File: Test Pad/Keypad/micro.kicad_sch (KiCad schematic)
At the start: 9 parts

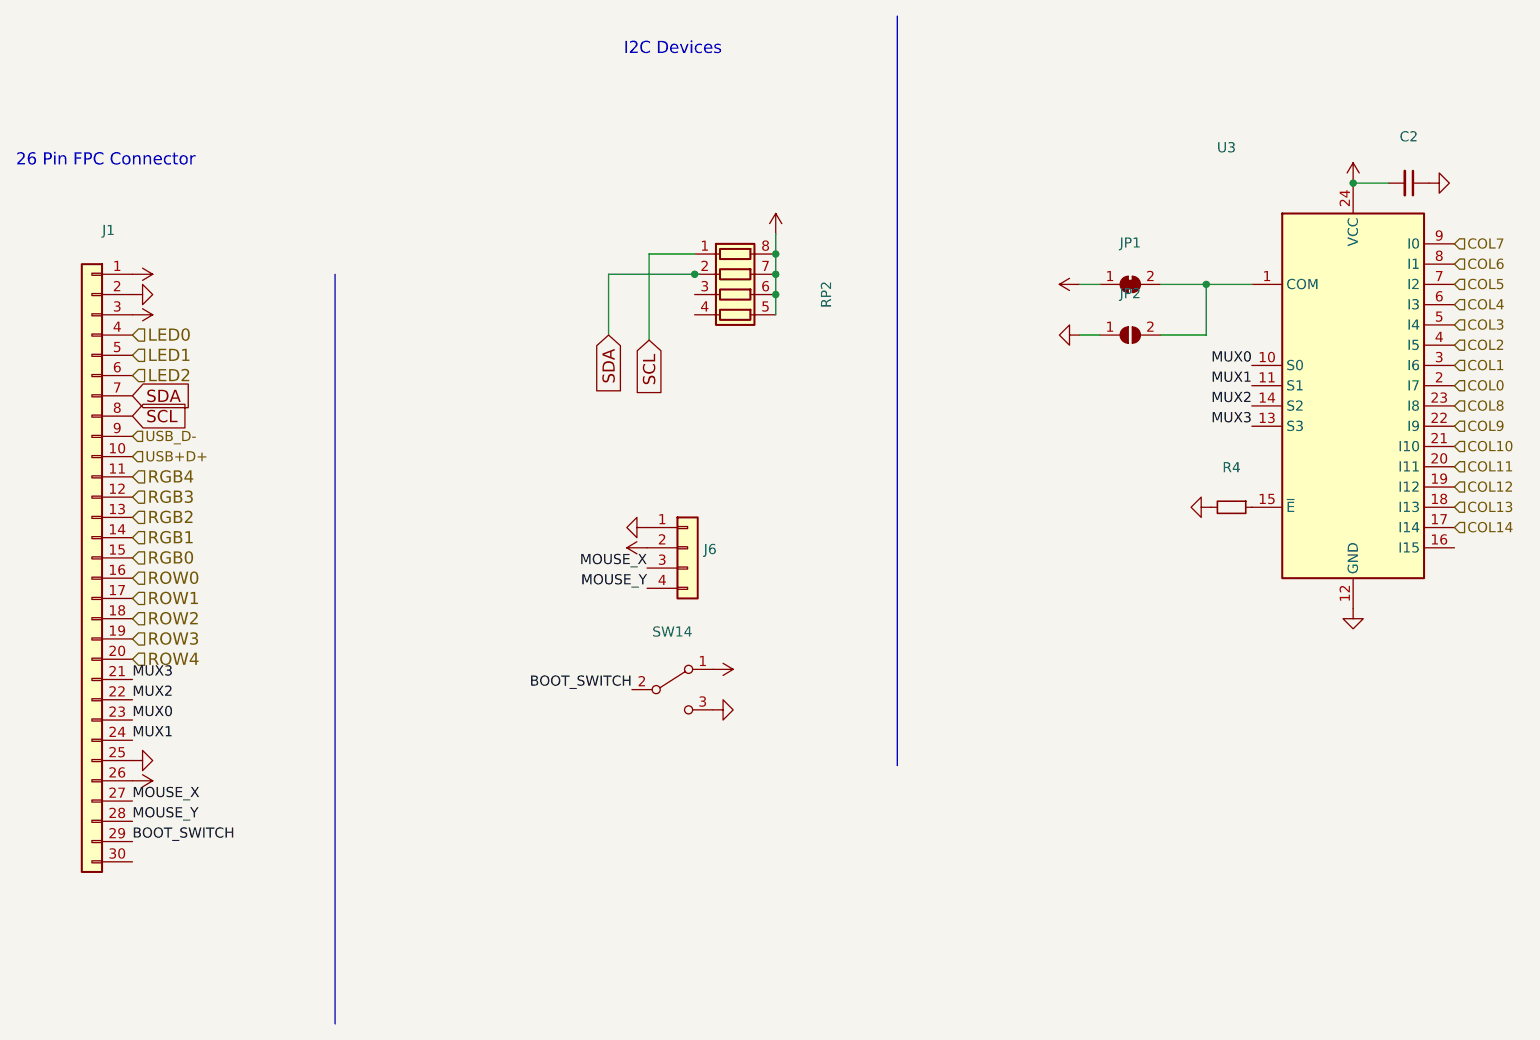
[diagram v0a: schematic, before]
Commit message: Started nucleo 144 test pad and keypad boards
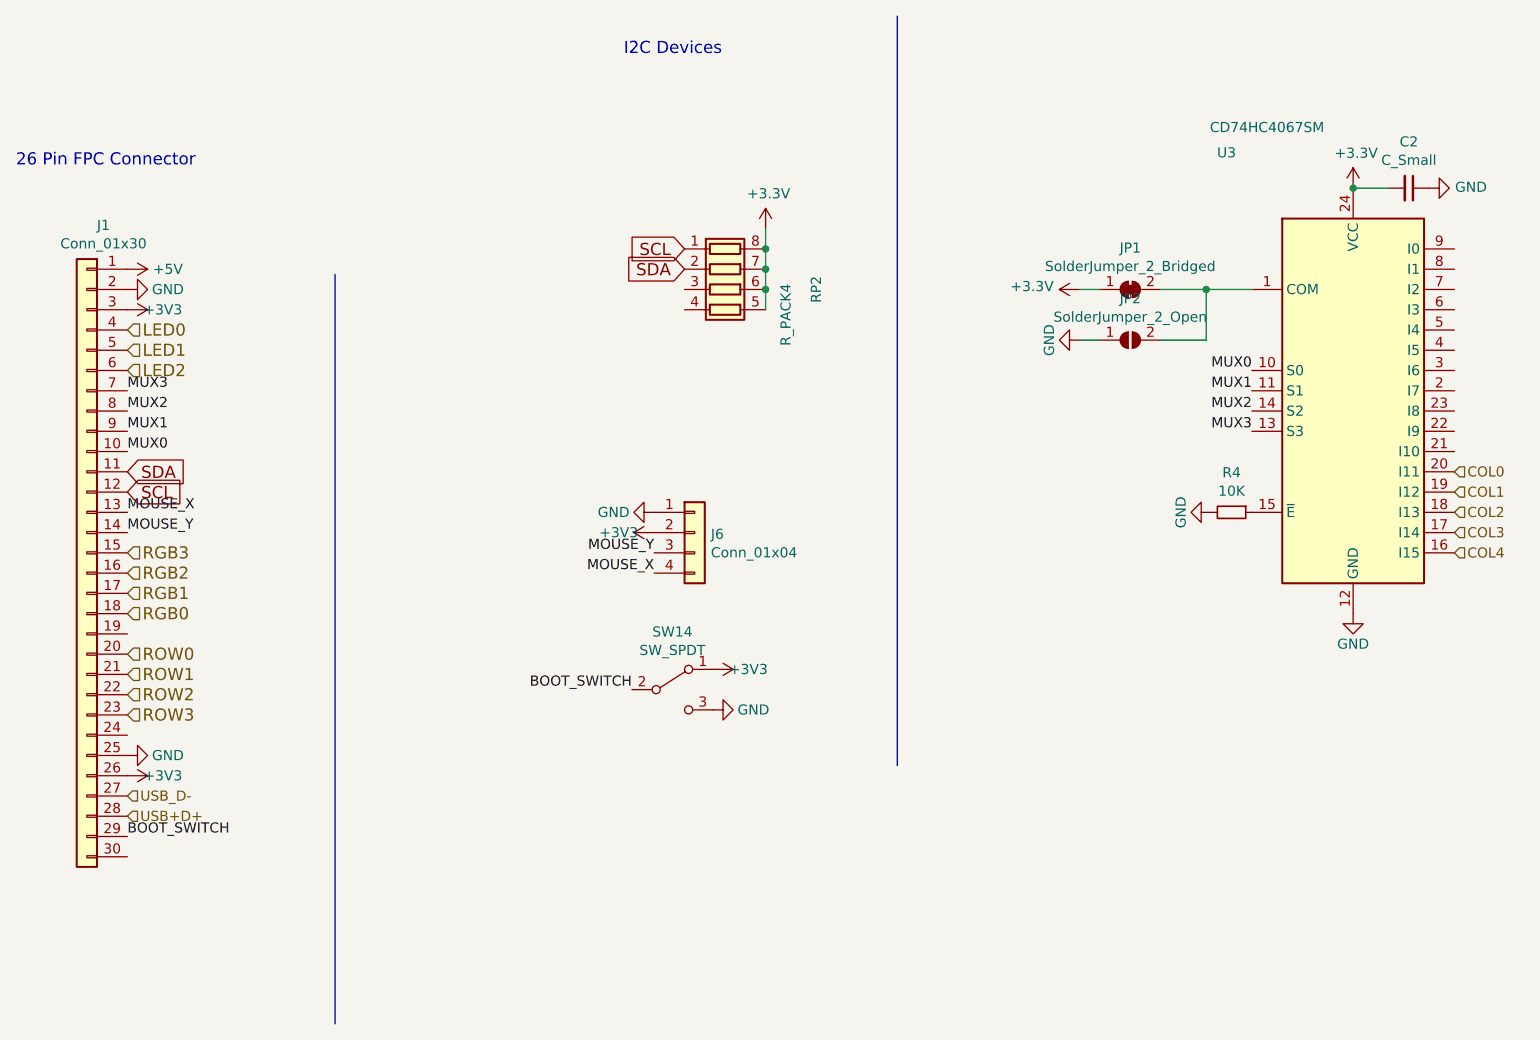
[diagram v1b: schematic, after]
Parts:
- C2: value (none) -> C_Small; footprint (none) -> Capacitor_SMD:C_0603_1608Metric
- J1: value (none) -> Conn_01x30; footprint (none) -> Connector_FFC-FPC:Hirose_FH12-30S-0.5SH_1x30-1MP_P0.50mm_Horizontal
- J6: value (none) -> Conn_01x04; footprint (none) -> Connector_JST:JST_PH_S4B-PH-SM4-TB_1x04-1MP_P2.00mm_Horizontal
- JP1: value (none) -> SolderJumper_2_Bridged; footprint (none) -> Jumper:SolderJumper-2_P1.3mm_Bridged_RoundedPad1.0x1.5mm
- JP2: value (none) -> SolderJumper_2_Open; footprint (none) -> Jumper:SolderJumper-2_P1.3mm_Open_RoundedPad1.0x1.5mm
- R4: value (none) -> 10K; footprint (none) -> Resistor_SMD:R_0603_1608Metric
- RP2: value (none) -> R_PACK4; footprint (none) -> Resistor_SMD:R_Array_Concave_4x0402
- SW14: value (none) -> SW_SPDT; footprint (none) -> keyboard:SS12F23
- U3: value (none) -> CD74HC4067SM; footprint (none) -> Package_SO:SSOP-24_5.3x8.2mm_P0.65mm
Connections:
- net COL11 is gone; now on net COL0: U3.20 (I11)
- net COL12 is gone; now on net COL1: U3.19 (I12)
- net COL13 is gone; now on net COL2: U3.18 (I13)
- net COL14 is gone; now on net COL3: U3.17 (I14)
- net RGB4 is gone; now on net SDA: J1.11 (Pin_11)
- net ROW4 is gone; now on net ROW0: J1.20 (Pin_20)
- net COL0: no longer U3.2 (I7)
- net COL1: no longer U3.3 (I6)
- net COL2: no longer U3.4 (I5)
- net COL3: no longer U3.5 (I4)
- net COL4: now also U3.16 (I15); no longer U3.6 (I3)
- net MOUSE_X: now also J1.13 (Pin_13), J6.4 (Pin_4); no longer J1.27 (Pin_27), J6.3 (Pin_3)
- net MOUSE_Y: now also J1.14 (Pin_14), J6.3 (Pin_3); no longer J1.28 (Pin_28), J6.4 (Pin_4)
- net MUX0: now also J1.10 (Pin_10); no longer J1.23 (Pin_23)
- net MUX1: now also J1.9 (Pin_9); no longer J1.24 (Pin_24)
- net MUX2: now also J1.8 (Pin_8); no longer J1.22 (Pin_22)
- net MUX3: now also J1.7 (Pin_7); no longer J1.21 (Pin_21)
- net RGB0: now also J1.18 (Pin_18); no longer J1.15 (Pin_15)
- net RGB1: now also J1.17 (Pin_17); no longer J1.14 (Pin_14)
- net RGB2: now also J1.16 (Pin_16); no longer J1.13 (Pin_13)
- net RGB3: now also J1.15 (Pin_15); no longer J1.12 (Pin_12)
- net ROW0: no longer J1.16 (Pin_16)
- net ROW1: now also J1.21 (Pin_21); no longer J1.17 (Pin_17)
- net ROW2: now also J1.22 (Pin_22); no longer J1.18 (Pin_18)
- net ROW3: now also J1.23 (Pin_23); no longer J1.19 (Pin_19)
- net SCL: now also J1.12 (Pin_12); no longer J1.8 (Pin_8)
- net SDA: no longer J1.7 (Pin_7)
- net USB+D+: now also J1.28 (Pin_28); no longer J1.10 (Pin_10)
- net USB_D-: now also J1.27 (Pin_27); no longer J1.9 (Pin_9)
- net COL10: no longer names the net of U3.21 (I10)
- net COL5: no longer names the net of U3.7 (I2)
- net COL6: no longer names the net of U3.8 (I1)
- net COL7: no longer names the net of U3.9 (I0)
- net COL8: no longer names the net of U3.23 (I8)
- net COL9: no longer names the net of U3.22 (I9)
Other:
- moved on the sheet: C2, J1, J6, JP1, JP2, R4, RP2, U3
